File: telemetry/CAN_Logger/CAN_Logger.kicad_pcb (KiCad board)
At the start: 2 copper layers, 109.3 x 58.3 mm, 56 parts, among them J1 CONN_02X03, J2 SD_socket, U1 MCP2561-E_SN, U101 TPS560430YF, U2 ATMEGA16M1, U3 LM3480, U4 TXB0104, U5 R_500, U6 R_500, U7 R_500, Y1 Crystal_SMD

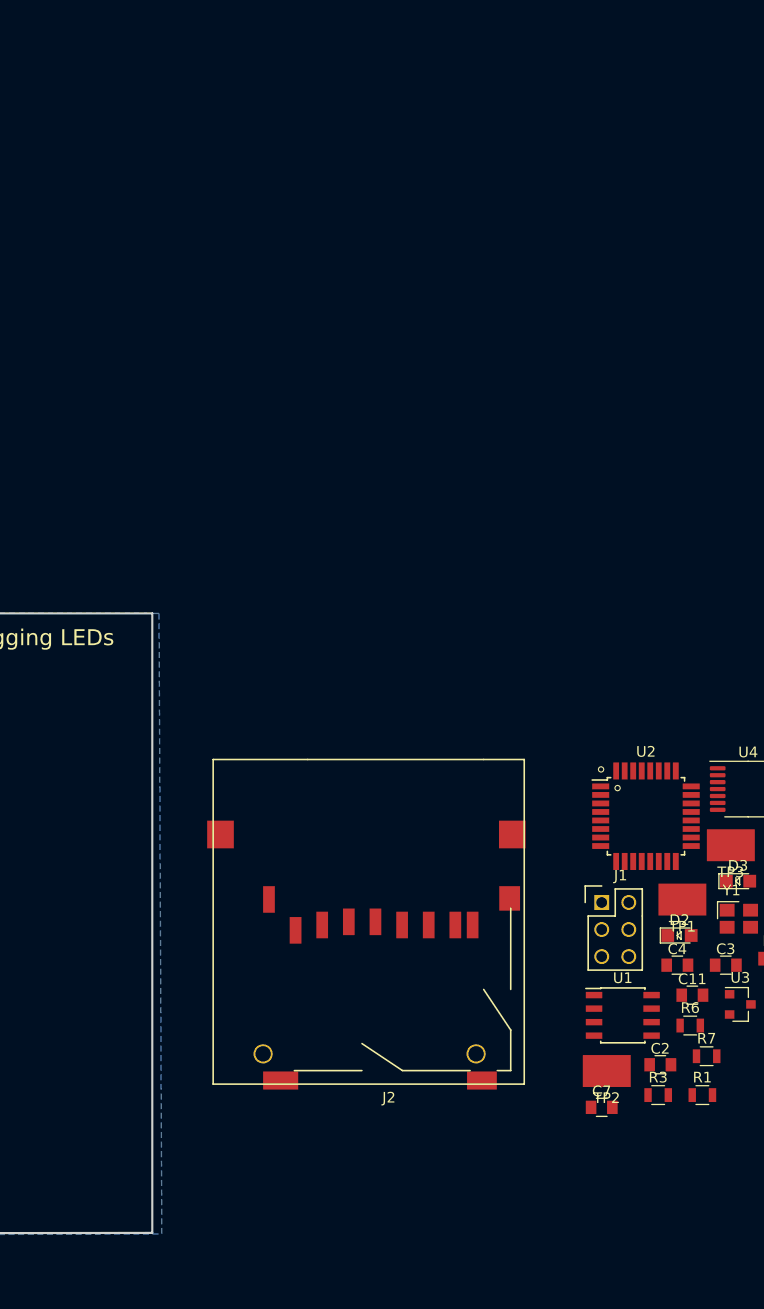
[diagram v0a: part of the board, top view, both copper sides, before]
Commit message: Small changes: 3.3V->3V3, added test points to Debug LEDS, etc.
Following recommendations given by Wesley, pg. 2 of this file:
https://drive.google.com/file/d/12oTchTOrF_66K-js-7AgllKoxS_4IslO/view.
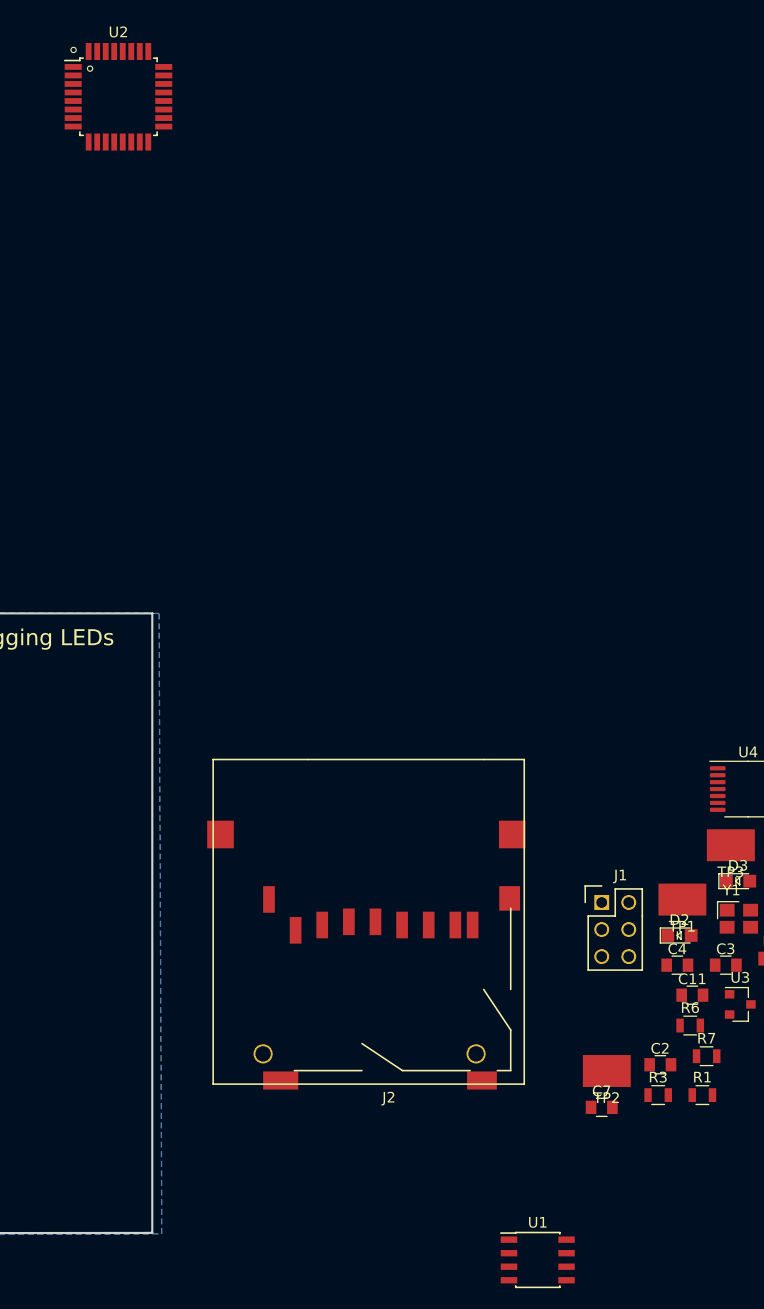
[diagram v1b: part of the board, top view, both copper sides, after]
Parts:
- moved U2 83.8 mm to (204.5, 27.9)
- moved U1 24.3 mm to (243.8, 137.2)
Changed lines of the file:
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@@
-(kicad_pcb (version 20171130) (host pcbnew 5.1.8-db9833491~88~ubuntu20.04.1)
+(kicad_pcb (version 20171130) (host pcbnew 5.1.9-73d0e3b20d~88~ubuntu20.04.1)
   (general
     (thickness 1.6)
@@
   )
   (setup
-    (last_trace_width 0.381)
+    (last_trace_width 0.1524)
     (user_trace_width 0.254)
     (user_trace_width 0.381)
@@
     (solder_mask_min_width 0.25)
     (aux_axis_origin 0 0)
-    (visible_elements FFFFFF7F)
+    (visible_elements FFFFF77F)
     (pcbplotparams
       (layerselection 0x010fc_ffffffff)
@@
   )
   (module footprints:SOIC-8_3.9x4.9mm_Pitch1.27mm_OEM (layer F.Cu)
-    (at 251.825001 114.195001)
+    (at 243.84 137.16)
     (descr "8-Lead Plastic Small Outline (SN) - Narrow, 3.90 mm Body [SOIC] (see Microchip Packaging Specification 00000049BS.pdf)")
     (tags "SOIC 1.27")
@@
   )
   (module footprints:TQFP-32_7x7mm_Pitch0.8mm (layer F.Cu)
-    (at 254 95.495001)
+    (at 204.47 27.94)
     (descr "32-Lead Plastic Thin Quad Flatpack (PT) - 7x7x1.0 mm Body, 2.00 mm [TQFP] (see Microchip Packaging Specification 00000049BS.pdf)")
     (tags "QFP 0.8")
@@
       (effects (font (size 1 1) (thickness 0.15)))
     )
-    (fp_text user %R (at 0 0) (layer F.Fab)
-      (effects (font (size 1 1) (thickness 0.15)))
-    )
     (fp_circle (center -2.667 -2.6416) (end -2.667 -2.6924) (layer F.SilkS) (width 0.5))
     (fp_circle (center -4.2164 -4.3942) (end -4.2164 -4.445) (layer F.SilkS) (width 0.5))
@@
     (fp_line (start 3.625 -3.625) (end 3.3 -3.625) (layer F.SilkS) (width 0.15))
     (fp_line (start -3.625 -3.4) (end -5.05 -3.4) (layer F.SilkS) (width 0.15))
+    (fp_text user %R (at 0 0) (layer F.Fab)
+      (effects (font (size 1 1) (thickness 0.15)))
+    )
     (pad 32 smd rect (at -2.8 -4.25 90) (size 1.6 0.55) (layers F.Cu F.Paste F.Mask)
       (net 52 "Net-(U2-Pad32)"))
@@
       (effects (font (size 1 1) (thickness 0.15)))
     )
-    (fp_text user %R (at 0 0 90) (layer F.Fab)
-      (effects (font (size 0.5 0.5) (thickness 0.075)))
-    )
     (fp_line (start -0.7 -0.95) (end -0.7 1.5) (layer F.Fab) (width 0.1))
     (fp_line (start -0.15 -1.52) (end 0.7 -1.52) (layer F.Fab) (width 0.1))
@@
     (fp_line (start 0.76 -1.58) (end -1.4 -1.58) (layer F.SilkS) (width 0.12))
     (fp_line (start 0.76 1.58) (end -0.7 1.58) (layer F.SilkS) (width 0.12))
+    (fp_text user %R (at 0 0 90) (layer F.Fab)
+      (effects (font (size 0.5 0.5) (thickness 0.075)))
+    )
     (pad 3 smd rect (at 1 0) (size 0.9 0.8) (layers F.Cu F.Paste F.Mask)
       (net 1 GND))
@@
       (effects (font (size 1 1) (thickness 0.15)))
     )
-    (fp_text user %R (at 0 0) (layer F.Fab)
-      (effects (font (size 1 1) (thickness 0.15)))
-    )
     (fp_line (start 0 2.61) (end 2.2 2.61) (layer F.SilkS) (width 0.12))
     (fp_line (start 0 2.61) (end -2.2 2.61) (layer F.SilkS) (width 0.12))
@@
     (fp_line (start 3.85 2.75) (end 3.85 -2.75) (layer F.CrtYd) (width 0.05))
     (fp_line (start 3.85 -2.75) (end -3.85 -2.75) (layer F.CrtYd) (width 0.05))
+    (fp_text user %R (at 0 0) (layer F.Fab)
+      (effects (font (size 1 1) (thickness 0.15)))
+    )
     (pad 14 smd roundrect (at 2.8625 -1.95) (size 1.475 0.4) (layers F.Cu F.Paste F.Mask) (roundrect_rratio 0.25)
       (net 10 +5V))
@@
   (segment (start 116.9543 101.6635) (end 115.4303 101.6635) (width 0.254) (layer F.Cu) (net 1))
   (segment (start 121.666 107.929) (end 108.606 107.929) (width 0.381) (layer F.Cu) (net 2))
-  (segment (start 123.1472 109.60608) (end 115.22828 117.525) (width 0.381) (layer F.Cu) (net 10))
-  (segment (start 124.0282 109.60608) (end 123.1472 109.60608) (width 0.381) (layer F.Cu) (net 10))
-  (segment (start 115.22828 117.525) (end 108.55 117.525) (width 0.381) (layer F.Cu) (net 10))
-  (segment (start 125.7 110.52388) (end 125.7 111.796) (width 0.254) (layer F.Cu) (net 10))
-  (segment (start 124.7822 109.60608) (end 125.7 110.52388) (width 0.254) (layer F.Cu) (net 10))
-  (segment (start 125.7 111.796) (end 125.7 112.4) (width 0.254) (layer F.Cu) (net 10))
-  (segment (start 124.0282 109.60608) (end 124.7822 109.60608) (width 0.254) (layer F.Cu) (net 10))
   (segment (start 116.90666 105.77514) (end 116.9543 105.7275) (width 0.381) (layer F.Cu) (net 3))
   (segment (start 125.7276 103.0658) (end 126.6776 103.0658) (width 0.381) (layer F.Cu) (net 3))
@@
   (segment (start 125.7276 99.6441) (end 125.7276 100.8658) (width 0.254) (layer F.Cu) (net 9))
   (segment (start 126.40822 98.96348) (end 125.7276 99.6441) (width 0.254) (layer F.Cu) (net 9))
+  (segment (start 123.1472 109.60608) (end 115.22828 117.525) (width 0.381) (layer F.Cu) (net 10))
+  (segment (start 124.0282 109.60608) (end 123.1472 109.60608) (width 0.381) (layer F.Cu) (net 10))
+  (segment (start 115.22828 117.525) (end 108.55 117.525) (width 0.381) (layer F.Cu) (net 10))
+  (segment (start 125.7 110.52388) (end 125.7 111.796) (width 0.254) (layer F.Cu) (net 10))
+  (segment (start 124.7822 109.60608) (end 125.7 110.52388) (width 0.254) (layer F.Cu) (net 10))
+  (segment (start 125.7 111.796) (end 125.7 112.4) (width 0.254) (layer F.Cu) (net 10))
+  (segment (start 124.0282 109.60608) (end 124.7822 109.60608) (width 0.254) (layer F.Cu) (net 10))
   (zone (net 1) (net_name GND) (layer F.Cu) (hatch edge 0.508)
     (connect_pads yes (clearance 0.1524))

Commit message: PCB Layout: grouped together functional blocks, added GND to connector
Grouped functional blocks together by component in PCB layout, connected connector to ground. Layout is currently off board.
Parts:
- added J3: MM_F_RA_20, footprints:micromatch_female_ra_20, F.Cu at (25.6, 36.0)
- added TP4: Test_Point_SMD, footprints:Test_Point_SMD, F.Cu at (69.7, 26.9)
- added TP5: Test_Point_SMD, footprints:Test_Point_SMD, F.Cu at (75.2, 26.9)
- added TP6: Test_Point_SMD, footprints:Test_Point_SMD, F.Cu at (80.7, 26.9)
- moved R2 193.4 mm to (92.7, 29.2)
- moved R1 193.0 mm to (92.7, 24.1)
- moved R3 183.9 mm to (94.0, 33.0)
- moved D1 181.7 mm to (101.6, 22.9)
- moved TP3 174.7 mm to (87.6, 109.2)
- moved D3 174.4 mm to (102.9, 31.8)
- moved D2 174.3 mm to (101.6, 27.9)
- moved TP1 169.9 mm to (87.6, 97.8)
- moved TP2 163.5 mm to (87.6, 102.9)
- moved U7 116.8 mm to (189.6, 24.1), turned to 180 degrees
- moved U6 116.0 mm to (193.4, 21.6), turned to 180 degrees
- moved U5 115.3 mm to (196.8, 20.3), turned to 180 degrees
- moved R7 113.8 mm to (205.7, 17.8)
- moved C2 108.2 mm to (196.6, 27.9), turned to 180 degrees
- moved R8 106.3 mm to (196.8, 30.5), turned to 180 degrees
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
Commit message: Worked PCB Layout, small schematic changes
+Layout: Everything on board, placed some wires and vias
+Schematic: Moved locations of P_LEDs on ATMEGA
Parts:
- removed the L101 at (270.9, 91.4)
- moved U3 200.7 mm to (118.1, 128.3), turned to 270 degrees
- moved C6 197.1 mm to (114.3, 128.3), turned to 270 degrees
- moved C7 197.0 mm to (121.9, 128.3), turned to 270 degrees
- moved R4 158.5 mm to (104.1, 102.9), turned to 180 degrees
- moved U1 153.5 mm to (104.1, 96.5), turned to 270 degrees
- moved C1 151.1 mm to (104.1, 90.2)
- moved C9 145.2 mm to (138.4, 100.3)
- moved U4 141.5 mm to (141.0, 96.5), turned to 180 degrees
- moved J1 140.3 mm to (142.2, 124.5)
- moved TP4 139.3 mm to (196.8, 83.8)
- moved TP5 136.6 mm to (196.8, 88.9)
- moved TP6 134.2 mm to (196.8, 94.0)
- moved C8 133.0 mm to (143.5, 100.3), turned to 180 degrees
- moved R1 123.4 mm to (200.7, 83.8), turned to 270 degrees
- moved R2 123.4 mm to (200.7, 88.9), turned to 270 degrees
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- renumbered U6 to R10, U7 to R11, U5 to R9
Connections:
- U2 pad 16: /P_LED_3 -> Net-(U2-Pad16)
- U2 pad 22: Net-(U2-Pad22) -> /P_LED_3
- U2 pad 23: Net-(U2-Pad23) -> /P_LED_2
- U2 pad 24: Net-(U2-Pad24) -> /P_LED_1
- U2 pad 8: /P_LED_1 -> Net-(U2-Pad8)
- U2 pad 9: /P_LED_2 -> Net-(U2-Pad9)
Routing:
- net GND: track 65.5 -> 151.7 mm, vias 11 -> 31
- net +3V3: track 0.00 -> 35.0 mm
- net +5V: track 22.7 -> 43.2 mm
- net /CAN_N: track 0.00 -> 15.3 mm
- net /CAN_RX: track 0.00 -> 14.7 mm
- net /12V: track 13.1 -> 25.2 mm
- net /CAN_P: track 0.00 -> 11.1 mm
- net /CAN_TX: track 0.00 -> 9.22 mm
- net /SD_DETECT: track 0.00 -> 5.42 mm
- net /MOSI: track 0.00 -> 3.91 mm
- net /SD_PROTECT: track 0.00 -> 2.65 mm
- net Net-(C3-Pad1): track 0.00 -> 2.24 mm
- net /MISO: track 0.00 -> 2.12 mm
- net Net-(C4-Pad1): track 0.00 -> 1.59 mm
- net Net-(C5-Pad1): track 0.00 -> 0.57 mm

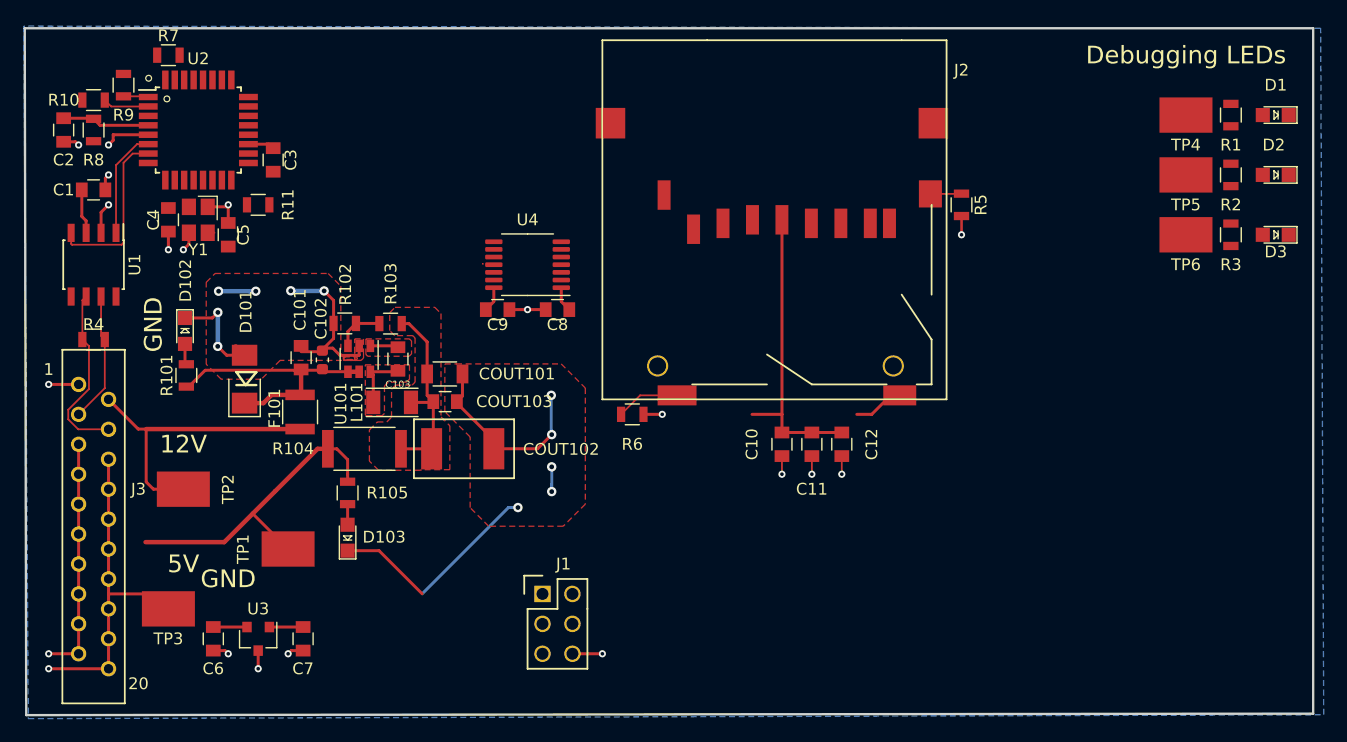
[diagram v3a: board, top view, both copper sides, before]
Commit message: Completed initial layout, wire connections
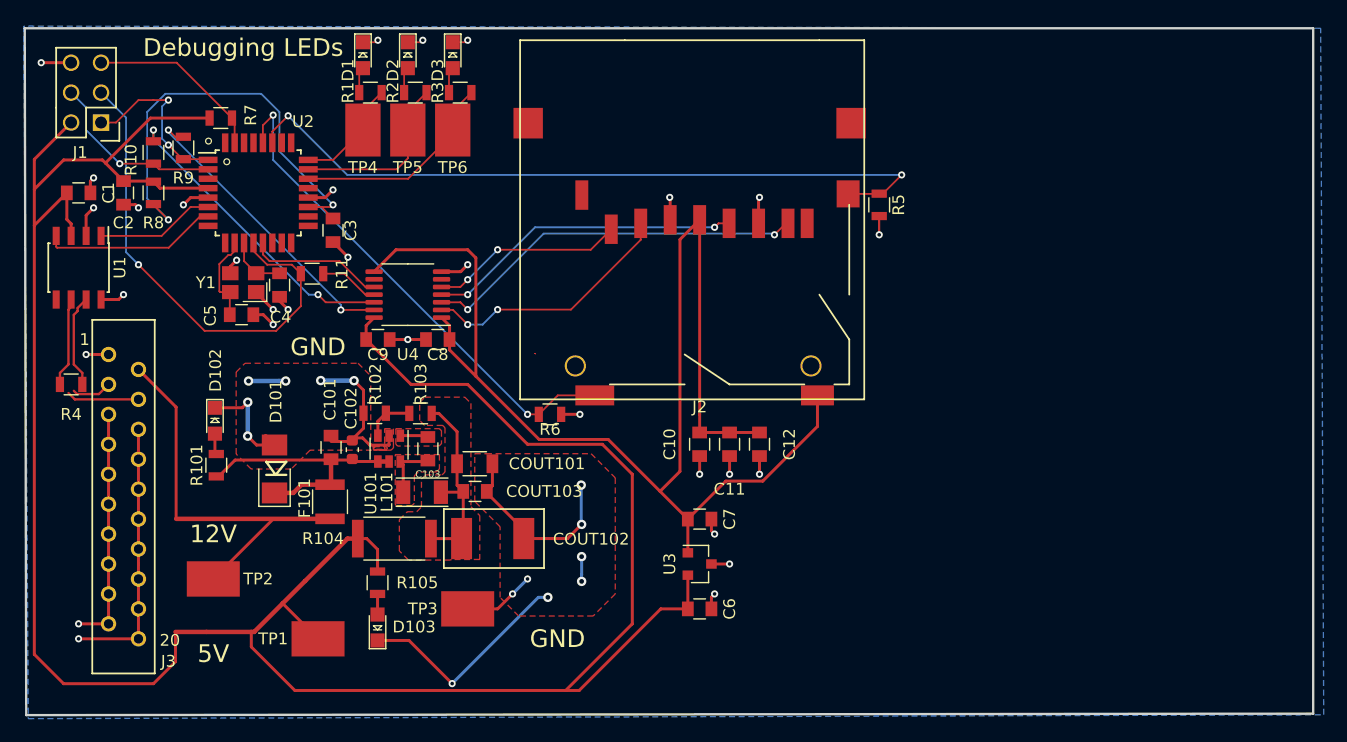
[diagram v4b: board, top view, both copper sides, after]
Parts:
- moved D1 77.6 mm to (127.0, 78.7), turned to 270 degrees
- moved D2 74.4 mm to (130.8, 78.7), turned to 270 degrees
- moved R1 73.0 mm to (127.6, 81.9), turned to 0 degrees
- moved D3 71.5 mm to (134.6, 78.7), turned to 270 degrees
- moved TP4 69.9 mm to (127.0, 85.1), turned to 270 degrees
- moved R2 69.6 mm to (131.4, 81.9), turned to 0 degrees
- moved R3 66.5 mm to (135.3, 81.9), turned to 0 degrees
- moved TP5 66.1 mm to (130.8, 85.1), turned to 270 degrees
- moved TP6 62.9 mm to (134.6, 85.1), turned to 270 degrees
- moved J1 54.8 mm to (104.8, 84.5), turned to 180 degrees
- moved C6 41.4 mm to (155.6, 125.7), turned to 0 degrees
- moved U3 38.0 mm to (155.6, 121.9), turned to 0 degrees
- moved C7 35.2 mm to (155.6, 118.1), turned to 0 degrees
- moved TP3 25.4 mm to (135.9, 125.7)
- moved C4 10.9 mm to (119.9, 98.2)
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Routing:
- net +5V: track 43.2 -> 220.7 mm
- net +3V3: track 35.0 -> 117.0 mm
- net /SD_PROTECT: track 2.65 -> 62.2 mm, vias 0 -> 2
- net /SCK: track 0.00 -> 41.2 mm, vias 0 -> 1
- net /SD_DETECT: track 5.42 -> 43.4 mm, vias 0 -> 2
- net Net-(C3-Pad1): track 2.24 -> 39.8 mm, vias 0 -> 2
- net /MOSI_3.3V: track 0.00 -> 32.8 mm, vias 0 -> 2
- net /SCK_3.3V: track 0.00 -> 26.9 mm, vias 0 -> 2
- net /MOSI_SD: track 0.00 -> 26.2 mm, vias 0 -> 2
- net /MISO_SD: track 0.00 -> 25.7 mm, vias 0 -> 2
- net /MISO_3.3V: track 0.00 -> 21.8 mm, vias 0 -> 2
- net /P_LED_3: track 0.00 -> 18.0 mm
- net /CS_3.3V: track 0.00 -> 16.4 mm, vias 0 -> 2
- net GND: track 151.7 -> 167.8 mm, vias 31 -> 44
- net /RESET: track 0.00 -> 15.2 mm
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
